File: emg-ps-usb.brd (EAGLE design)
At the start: 58.4 x 19.1 mm, 14 parts, among them U2 PHONE_JACK_MONO, X1 53047-04

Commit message: Cleaned up layout and routing. Moved LED to top and removed UCDRASCAL logo.
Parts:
- removed U$1: UCDAVIS-RASCAL_LOGO-2LINE, ucdrascal-eagle-lib:UCDAVIS-RASCAL_LOGO
- moved D1 19.1 mm to (21.6, 16.5), flipped to the top, turned to 180 degrees
- moved R1 2.54 mm to (18.4, 16.5), turned to 270 degrees
- moved U2 1.27 mm to (58.4, 3.81)
- moved JP2 0.25 mm to (52.7, 17.5)
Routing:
- net N$3: track 18.6 -> 3.24 mm, vias 1 -> 0
- net GND: track 8.81 -> 0.00 mm
- net SIG: track 13.7 -> 10.7 mm
- net VBUS: track 31.1 -> 28.7 mm
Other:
- board text added: "D1"
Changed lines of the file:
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@@
 <setting verticaltext="up"/>
 </settings>
-<grid distance="0.1" unitdist="inch" unit="inch" style="lines" multiple="1" display="yes" altdistance="0.005" altunitdist="inch" altunit="inch"/>
+<grid distance="0.025" unitdist="inch" unit="inch" style="lines" multiple="1" display="yes" altdistance="0.005" altunitdist="inch" altunit="inch"/>
 <layers>
 <layer number="1" name="Top" color="4" fill="1" visible="yes" active="yes"/>
@@
 <text x="42.926" y="13.97" size="1.016" layer="21" font="vector" ratio="10" align="center-right">GND</text>
 <text x="42.926" y="12.7" size="1.016" layer="21" font="vector" ratio="10" align="center-right">-VE</text>
+<text x="22.225" y="16.51" size="0.8128" layer="25" font="vector" align="center-left">D1</text>
 </plain>
 <attributes>
@@
 <description language="de">&lt;b&gt;EAGLE Design Rules&lt;/b&gt;
 &lt;p&gt;
-Die Standard-Design-Rules sind so gewÃ¤hlt, dass sie fÃ¼r
+Die Standard-Design-Rules sind so gewählt, dass sie für
 die meisten Anwendungen passen. Sollte ihre Platine
 besondere Anforderungen haben, treffen Sie die erforderlichen
@@
 <elements>
 <element name="U$2" library="eagle-lib" package="SOIC8" value="ADM660ARZ" x="23.495" y="9.525" smashed="yes" rot="R270"/>
-<element name="R1" library="SparkFun-Resistors" package="0805" value="1k" x="20.955" y="16.51" smashed="yes" rot="R180">
-<attribute name="NAME" x="21.082" y="15.621" size="0.8128" layer="25" font="vector" align="top-center"/>
-</element>
-<element name="D1" library="SparkFun-LED" package="LED-0603" value="RED" x="40.64" y="17.78" smashed="yes" rot="MR90">
-<attribute name="PROD_ID" value="DIO-00819" x="-15.24" y="59.69" size="1.778" layer="28" rot="MR90" display="off"/>
+<element name="R1" library="SparkFun-Resistors" package="0805" value="1k" x="18.415" y="16.51" smashed="yes" rot="R270">
+<attribute name="NAME" x="17.78" y="16.51" size="0.8128" layer="25" font="vector" rot="R180" align="center-left"/>
+</element>
+<element name="D1" library="SparkFun-LED" package="LED-0603" value="RED" x="21.59" y="16.51" smashed="yes" rot="R180">
+<attribute name="PROD_ID" value="DIO-00819" x="-20.32" y="72.39" size="1.778" layer="27" rot="R180" display="off"/>
 </element>
 <element name="C1" library="SparkFun-Capacitors" package="0805" value="10uF" x="17.145" y="8.89" smashed="yes" rot="R270">
@@
 <attribute name="OC_FARNELL" value="9733060" x="101.6" y="-20.955" size="1.778" layer="28" rot="MR270" display="off"/>
 </element>
-<element name="JP2" library="eagle-lib" package="TE-284093" value="TE-284093" x="52.705" y="17.78" smashed="yes" rot="MR180"/>
+<element name="JP2" library="eagle-lib" package="TE-284093" value="TE-284093" x="52.705" y="17.526" smashed="yes" rot="MR180"/>
 <element name="S1" library="SparkFun-Electromechanical" package="SWITCH-SPST-SMD-A" value="SPDT" x="11.43" y="17.145" smashed="yes"/>
 <element name="JP1" library="SparkFun-Connectors" package="USB-A-H" value="USB-A-H" x="3.175" y="9.525" smashed="yes" rot="MR180"/>
-<element name="U2" library="eagle-lib" package="MJ-3523-SMT" value="PHONE_JACK_MONO" x="58.42" y="5.08" smashed="yes"/>
-<element name="U$1" library="ucdrascal-eagle-lib" package="UCDAVIS-RASCAL_LOGO" value="UCDAVIS-RASCAL_LOGO-2LINE" x="51.562" y="13.462"/>
+<element name="U2" library="eagle-lib" package="MJ-3523-SMT" value="PHONE_JACK_MONO" x="58.42" y="3.81" smashed="yes"/>
 <element name="U$3" library="ucdrascal-eagle-lib" package="EMG_Y03_OUTLINEENDS" value="EMG_AMP_OUTLINE-Y03ENDS" x="44.958" y="-0.254" rot="MR0"/>
 </elements>
@@
 <vertex x="58.42" y="0"/>
 </polygon>
-<wire x1="41.39" y1="17.78" x2="50.205" y2="17.78" width="0.4064" layer="16"/>
 </signal>
 <signal name="VBUS">
@@
 <wire x1="26.1112" y1="11.43" x2="26.1112" y2="13.2588" width="0.6096" layer="1"/>
 <wire x1="26.1112" y1="13.2588" x2="25.4" y2="13.97" width="0.6096" layer="1"/>
-<wire x1="25.4" y1="13.97" x2="17.78" y2="13.97" width="0.6096" layer="1"/>
-<wire x1="20.055" y1="16.51" x2="19.05" y2="16.51" width="0.4064" layer="1"/>
-<wire x1="19.05" y1="16.51" x2="17.78" y2="15.24" width="0.4064" layer="1"/>
-<wire x1="17.78" y1="15.24" x2="17.78" y2="13.97" width="0.4064" layer="1"/>
+<wire x1="25.4" y1="13.97" x2="18.415" y2="13.97" width="0.6096" layer="1"/>
+<wire x1="18.415" y1="13.97" x2="14.224" y2="13.97" width="0.6096" layer="1"/>
 <wire x1="13.68" y1="15.395" x2="13.68" y2="14.514" width="0.6096" layer="1"/>
 <wire x1="13.68" y1="14.514" x2="14.224" y2="13.97" width="0.6096" layer="1"/>
-<wire x1="14.224" y1="13.97" x2="17.78" y2="13.97" width="0.6096" layer="1"/>
+<wire x1="18.415" y1="15.61" x2="18.415" y2="13.97" width="0.4064" layer="1"/>
 </signal>
 <signal name="N$3">
 <contactref element="R1" pad="1"/>
 <contactref element="D1" pad="A"/>
-<wire x1="21.855" y1="16.51" x2="25.4" y2="16.51" width="0.4064" layer="1"/>
-<via x="25.4" y="16.51" extent="1-16" drill="0.6"/>
-<wire x1="25.4" y1="16.51" x2="26.67" y2="16.51" width="0.4064" layer="16"/>
-<wire x1="26.67" y1="16.51" x2="27.94" y2="17.78" width="0.4064" layer="16"/>
-<wire x1="27.94" y1="17.78" x2="39.89" y2="17.78" width="0.4064" layer="16"/>
+<wire x1="18.415" y1="17.41" x2="21.44" y2="17.41" width="0.4064" layer="1"/>
+<wire x1="21.44" y1="17.41" x2="21.59" y2="17.26" width="0.4064" layer="1"/>
 </signal>
 <signal name="SIG">
 <contactref element="U2" pad="P$2"/>
 <contactref element="X1" pad="4"/>
-<wire x1="44" y1="16.48" x2="48.23" y2="16.48" width="0.4064" layer="1"/>
-<wire x1="48.23" y1="16.48" x2="48.26" y2="16.51" width="0.4064" layer="1"/>
-<wire x1="48.26" y1="16.51" x2="49.53" y2="15.24" width="0.4064" layer="1"/>
-<wire x1="49.53" y1="15.24" x2="49.53" y2="11.69" width="0.4064" layer="1"/>
-<wire x1="49.53" y1="11.69" x2="46.62" y2="8.78" width="0.4064" layer="1"/>
+<wire x1="44" y1="16.48" x2="45.115" y2="16.48" width="0.4064" layer="1"/>
+<wire x1="45.115" y1="16.48" x2="46.355" y2="15.24" width="0.4064" layer="1"/>
+<wire x1="46.355" y1="15.24" x2="46.355" y2="7.775" width="0.4064" layer="1"/>
+<wire x1="46.355" y1="7.775" x2="46.62" y2="7.51" width="0.4064" layer="1"/>
 </signal>
 <signal name="N$4">

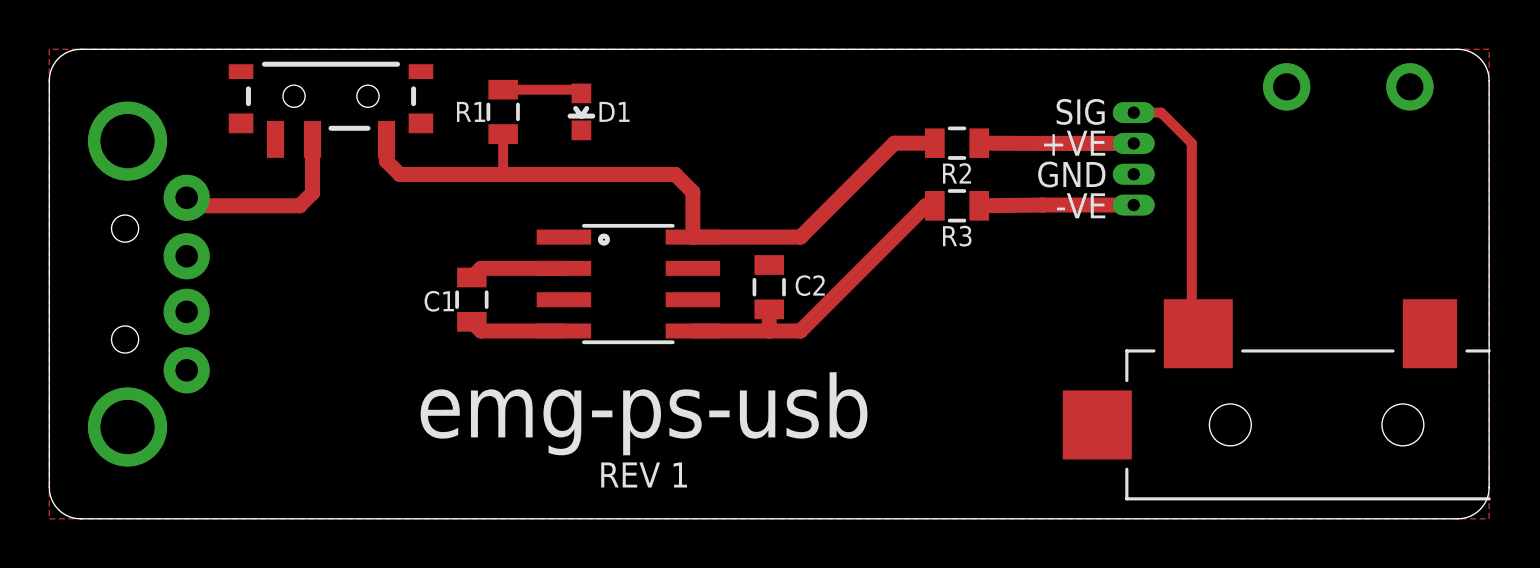
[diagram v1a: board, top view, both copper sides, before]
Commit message: Added UCDRASCAL logo. Swapped the 4x1 Molex connector for just a wire to board interface. Updated BOM.
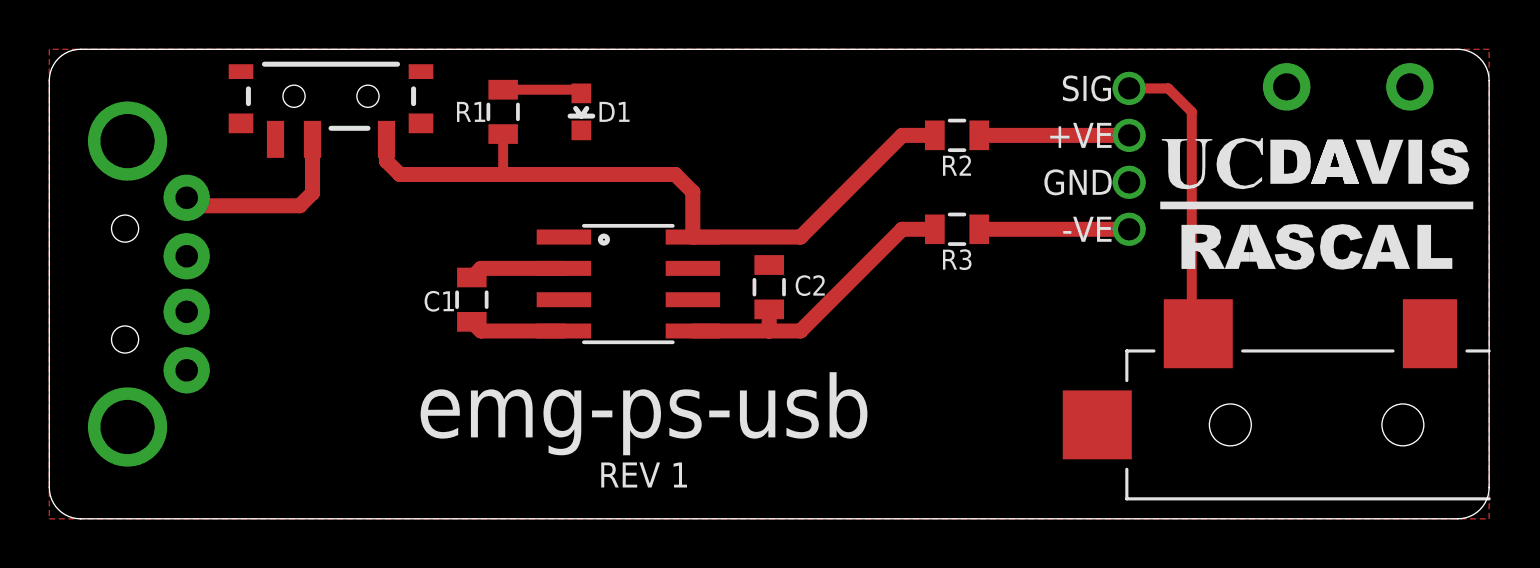
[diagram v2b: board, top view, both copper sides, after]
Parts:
- removed X1: 53047-04, con-molex:53047-04
- added J1: AMPLIFIER_Y03, eagle-lib:AMPLIFIER_WTB
- added U$1: UCDAVIS-RASCAL_LOGO-2LINE, ucdrascal-eagle-lib:UCDAVIS-RASCAL_LOGO
- moved R3 0.95 mm to (36.8, 11.7)
- moved R2 0.32 mm to (36.8, 15.6)
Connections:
- net +VE: now also J1.3; no longer X1.3
- net -VE: now also J1.1; no longer X1.1
- net GND: now also J1.2; no longer X1.2
- net SIG: now also J1.4; no longer X1.4
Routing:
- net SIG: track 10.7 -> 12.0 mm
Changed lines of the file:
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@@
 <setting verticaltext="up"/>
 </settings>
-<grid distance="0.025" unitdist="inch" unit="inch" style="lines" multiple="1" display="yes" altdistance="0.005" altunitdist="inch" altunit="inch"/>
+<grid distance="0.635" unitdist="mm" unit="mm" style="lines" multiple="1" display="yes" altdistance="0.00125" altunitdist="inch" altunit="inch"/>
 <layers>
 <layer number="1" name="Top" color="4" fill="1" visible="yes" active="yes"/>
@@
 <layer number="27" name="tValues" color="7" fill="1" visible="yes" active="yes"/>
 <layer number="28" name="bValues" color="7" fill="1" visible="yes" active="yes"/>
-<layer number="29" name="tStop" color="7" fill="3" visible="yes" active="yes"/>
-<layer number="30" name="bStop" color="7" fill="6" visible="yes" active="yes"/>
+<layer number="29" name="tStop" color="7" fill="3" visible="no" active="yes"/>
+<layer number="30" name="bStop" color="7" fill="6" visible="no" active="yes"/>
 <layer number="31" name="tCream" color="7" fill="4" visible="no" active="yes"/>
 <layer number="32" name="bCream" color="7" fill="5" visible="no" active="yes"/>
@@
 <text x="24.13" y="3.302" size="2.54" layer="21" font="vector" ratio="13" rot="SR0" align="bottom-center">emg-ps-usb</text>
 <text x="24.13" y="1.27" size="1.016" layer="21" font="vector" ratio="10" align="bottom-center">REV 1</text>
-<text x="42.926" y="16.51" size="1.016" layer="21" font="vector" ratio="10" align="center-right">SIG</text>
-<text x="42.926" y="15.24" size="1.016" layer="21" font="vector" ratio="10" align="center-right">+VE</text>
-<text x="42.926" y="13.97" size="1.016" layer="21" font="vector" ratio="10" align="center-right">GND</text>
-<text x="42.926" y="12.7" size="1.016" layer="21" font="vector" ratio="10" align="center-right">-VE</text>
+<text x="43.18" y="17.4625" size="1.016" layer="21" font="vector" ratio="10" align="center-right">SIG</text>
+<text x="43.18" y="15.5575" size="1.016" layer="21" font="vector" ratio="10" align="center-right">+VE</text>
+<text x="43.18" y="13.6525" size="1.016" layer="21" font="vector" ratio="10" align="center-right">GND</text>
+<text x="43.18" y="11.7475" size="1.016" layer="21" font="vector" ratio="10" align="center-right">-VE</text>
 <text x="22.225" y="16.51" size="0.8128" layer="25" font="vector" align="center-left">D1</text>
 </plain>
@@
 <attribute name="NAME" x="30.226" y="9.4615" size="0.8128" layer="25" font="vector" align="center-left"/>
 </element>
-<element name="R2" library="SparkFun-Resistors" package="0805" value="100" x="36.83" y="15.24" smashed="yes">
-<attribute name="NAME" x="36.83" y="14.4145" size="0.8128" layer="25" font="vector" align="top-center"/>
-</element>
-<element name="R3" library="SparkFun-Resistors" package="0805" value="100" x="36.83" y="12.7" smashed="yes">
-<attribute name="NAME" x="36.83" y="11.8745" size="0.8128" layer="25" font="vector" align="top-center"/>
-</element>
-<element name="X1" library="con-molex" package="53047-04" value="53047-04" x="44.45" y="14.605" smashed="yes" rot="MR270">
-<attribute name="OC_NEWARK" value="38C9900" x="101.6" y="-20.955" size="1.778" layer="28" rot="MR270" display="off"/>
-<attribute name="MPN" value="53047-0410" x="101.6" y="-20.955" size="1.778" layer="28" rot="MR270" display="off"/>
-<attribute name="MF" value="WALDOM/MOLEX" x="101.6" y="-20.955" size="1.778" layer="28" rot="MR270" display="off"/>
-<attribute name="OC_FARNELL" value="9733060" x="101.6" y="-20.955" size="1.778" layer="28" rot="MR270" display="off"/>
+<element name="R2" library="SparkFun-Resistors" package="0805" value="100" x="36.83" y="15.5575" smashed="yes">
+<attribute name="NAME" x="36.83" y="14.732" size="0.8128" layer="25" font="vector" align="top-center"/>
+</element>
+<element name="R3" library="SparkFun-Resistors" package="0805" value="100" x="36.83" y="11.7475" smashed="yes">
+<attribute name="NAME" x="36.83" y="10.922" size="0.8128" layer="25" font="vector" align="top-center"/>
 </element>
 <element name="JP2" library="eagle-lib" package="TE-284093" value="TE-284093" x="52.705" y="17.526" smashed="yes" rot="MR180"/>
@@
 <element name="U2" library="eagle-lib" package="MJ-3523-SMT" value="PHONE_JACK_MONO" x="58.42" y="3.81" smashed="yes"/>
 <element name="U$3" library="ucdrascal-eagle-lib" package="EMG_Y03_OUTLINEENDS" value="EMG_AMP_OUTLINE-Y03ENDS" x="44.958" y="-0.254" rot="MR0"/>
+<element name="J1" library="eagle-lib" package="AMPLIFIER_WTB" value="AMPLIFIER_Y03" x="43.815" y="14.605" rot="R90"/>
+<element name="U$1" library="ucdrascal-eagle-lib" package="UCDAVIS-RASCAL_LOGO" value="UCDAVIS-RASCAL_LOGO-2LINE" x="51.435" y="12.7"/>
 </elements>
 <signals>
@@
 <contactref element="C2" pad="2"/>
 <contactref element="U$2" pad="3"/>
-<contactref element="X1" pad="2"/>
 <contactref element="JP2" pad="P$1"/>
 <contactref element="JP2" pad="P$2"/>
@@
 <vertex x="58.42" y="0"/>
 </polygon>
+<contactref element="J1" pad="2"/>
 </signal>
 <signal name="VBUS">
@@
 <contactref element="U$2" pad="8"/>
 <contactref element="R2" pad="1"/>
-<wire x1="35.93" y1="15.24" x2="34.29" y2="15.24" width="0.6096" layer="1"/>
-<wire x1="34.29" y1="15.24" x2="30.48" y2="11.43" width="0.6096" layer="1"/>
 <wire x1="30.48" y1="11.43" x2="26.1112" y2="11.43" width="0.6096" layer="1"/>
 <wire x1="26.1112" y1="11.43" x2="26.1112" y2="13.2588" width="0.6096" layer="1"/>
@@
 <wire x1="13.68" y1="14.514" x2="14.224" y2="13.97" width="0.6096" layer="1"/>
 <wire x1="18.415" y1="15.61" x2="18.415" y2="13.97" width="0.4064" layer="1"/>
+<wire x1="35.93" y1="15.5575" x2="34.6075" y2="15.5575" width="0.6096" layer="1"/>
+<wire x1="34.6075" y1="15.5575" x2="30.48" y2="11.43" width="0.6096" layer="1"/>
 </signal>
 <signal name="N$3">
@@
 <signal name="SIG">
 <contactref element="U2" pad="P$2"/>
-<contactref element="X1" pad="4"/>
-<wire x1="44" y1="16.48" x2="45.115" y2="16.48" width="0.4064" layer="1"/>
-<wire x1="45.115" y1="16.48" x2="46.355" y2="15.24" width="0.4064" layer="1"/>
-<wire x1="46.355" y1="15.24" x2="46.355" y2="7.775" width="0.4064" layer="1"/>
+<wire x1="46.355" y1="16.51" x2="46.355" y2="7.775" width="0.4064" layer="1"/>
 <wire x1="46.355" y1="7.775" x2="46.62" y2="7.51" width="0.4064" layer="1"/>
+<contactref element="J1" pad="4"/>
+<wire x1="43.815" y1="17.4625" x2="45.4025" y2="17.4625" width="0.4064" layer="1"/>
+<wire x1="45.4025" y1="17.4625" x2="46.355" y2="16.51" width="0.4064" layer="1"/>
 </signal>
 <signal name="N$4">
@@
 <contactref element="R3" pad="1"/>
 <contactref element="C2" pad="1"/>
-<wire x1="35.93" y1="12.7" x2="35.56" y2="12.7" width="0.6096" layer="1"/>
-<wire x1="35.56" y1="12.7" x2="30.48" y2="7.62" width="0.6096" layer="1"/>
 <wire x1="30.48" y1="7.62" x2="29.21" y2="7.62" width="0.6096" layer="1"/>
 <wire x1="29.21" y1="7.62" x2="26.1112" y2="7.62" width="0.6096" layer="1"/>
 <wire x1="29.21" y1="8.498" x2="29.21" y2="7.62" width="0.6096" layer="1"/>
+<wire x1="35.93" y1="11.7475" x2="34.6075" y2="11.7475" width="0.6096" layer="1"/>
+<wire x1="34.6075" y1="11.7475" x2="30.48" y2="7.62" width="0.6096" layer="1"/>
 </signal>
 <signal name="+VE">
 <contactref element="R2" pad="2"/>
-<contactref element="X1" pad="3"/>
-<wire x1="44" y1="15.23" x2="40.28" y2="15.23" width="0.6096" layer="1"/>
-<wire x1="40.28" y1="15.23" x2="37.73" y2="15.24" width="0.6096" layer="1"/>
+<contactref element="J1" pad="3"/>
+<wire x1="37.73" y1="15.5575" x2="43.815" y2="15.5575" width="0.6096" layer="1"/>
 </signal>
 <signal name="-VE">
 <contactref element="R3" pad="2"/>
-<contactref element="X1" pad="1"/>
-<wire x1="44" y1="12.73" x2="40.3" y2="12.73" width="0.6096" layer="1"/>
-<wire x1="40.3" y1="12.73" x2="37.73" y2="12.7" width="0.6096" layer="1"/>
+<contactref element="J1" pad="1"/>
+<wire x1="37.73" y1="11.7475" x2="43.815" y2="11.7475" width="0.6096" layer="1"/>
 </signal>
 <signal name="N$5">
